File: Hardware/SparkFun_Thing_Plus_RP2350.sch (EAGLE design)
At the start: 78 parts, among them J1 THING_PLUS_LOGICAL, J3 QWIIC_RIGHT_ANGLE, J6 MICRO-SDFRICTION, Q1 100mA/20V/3.8Ω, U1 RP2350A, U2 RM2, U3 RT9080-33GJ5, U4 LM66200, U5 W25QXX128MBIT, U6 MCP73831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

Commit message: Update Eagle libs
Add PROD_ID for RM2
Update Eagle libs for updated version of RT9080 and LM66200
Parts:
- U3: device SparkFun-IC-Power:V_REG_RT9080 -> SparkFun-IC-Power:V_REG_RT9080-33GJ5
- U4: device SparkFun_Thing_Plus_RA6M5:IDEAL_DIODE_DUAL_LM66200 -> SparkFun-IC-Power:IDEAL_DIODE_DUAL_LM66200
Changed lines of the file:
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@@
 <part name="I2C" library="SparkFun-Jumpers" deviceset="JUMPER-SMT_3_2-NC_TRACE" device="_SILK" package3d_urn="urn:adsk.eagle:package:39289/1"/>
 <part name="SUPPLY11" library="SparkFun-PowerSymbols" deviceset="3.3V" device=""/>
-<part name="U3" library="SparkFun-IC-Power" deviceset="V_REG_RT9080" device="" value="RT9080-33GJ5"/>
+<part name="U3" library="SparkFun-IC-Power" deviceset="V_REG_RT9080-33GJ5" device="" value="RT9080-33GJ5"/>
 <part name="C1" library="SparkFun-Capacitors" deviceset="2.2UF" device="-0402_TIGHT-10V-10%-X5R" value="2.2uF"/>
 <part name="C2" library="SparkFun-Capacitors" deviceset="2.2UF" device="-0402_TIGHT-10V-10%-X5R" value="2.2uF"/>
@@
 <part name="SUPPLY12" library="SparkFun-PowerSymbols" deviceset="3.3V" device=""/>
 <part name="R7" library="SparkFun-Resistors" deviceset="1MOHM" device="-0402T-1/16W-5%" value="1M"/>
-<part name="U4" library="SparkFun_Thing_Plus_RA6M5" deviceset="IDEAL_DIODE_DUAL_LM66200" device="" value="LM66200"/>
+<part name="U4" library="SparkFun-IC-Power" deviceset="IDEAL_DIODE_DUAL_LM66200" device="" value="LM66200"/>
 <part name="GND14" library="SparkFun-PowerSymbols" deviceset="GND" device=""/>
 <part name="R8" library="SparkFun-Resistors" deviceset="10KOHM" device="-0402T-1/16W-1%" value="10k"/>

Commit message: Remove SD card SDIO
SDIO can only be achieved via the PIO, and support for it is questionable. Changing to SPI frees up 5 GPIO that can be used for other purposes.
Change SD card socket to CONN-20948
Connect SPI pins to SD card socket
Connect SD card detection pin to GPIO pin
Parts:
- J6: value MICRO-SDFRICTION -> MICRO-SD-ATOM; device SparkFun-Connectors:MICRO-SDFRICTION -> SparkFun-Connectors:MICRO-SD-ATOM
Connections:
- net SD_!CS!/D3 renamed SD_!CS!
- removed net SD_D1: J6.DAT1, U1.GPIO11
- removed net SD_D2: J6.DAT2, U1.GPIO10
- removed net SD_PICO/CMD: J6.CMD/SDI, U1.GPIO15
- removed net SD_POCI/D0: J6.DAT0/SDO, U1.GPIO12
- removed net SD_SCLK: J6.CLK/SCK, U1.GPIO14
- new net !SD_DET!: J6.!DET!, U1.GPIO10
- net 3.3V: now also J6.VDD; no longer J6.VCC
- net GND: now also J6.SHIELD, J6.VSS; no longer J6.GND
- net PICO: now also J6.CMD/SDI
- net POCI: now also J6.DAT0/SDO
- net SCK: now also J6.CLK/SCK
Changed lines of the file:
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@@
 <part name="SUPPLY37" library="SparkFun-PowerSymbols" deviceset="VDDA" device=""/>
 <part name="L1" library="SparkFun-Coils" deviceset="4.7μH_SHIELDED_INDUCTOR" device="" value="4.7μH"/>
-<part name="J6" library="SparkFun-Connectors" deviceset="MICRO-SD" device="FRICTION"/>
 <part name="R18" library="SparkFun-Resistors" deviceset="10OHM" device="-0402-1/16W-5%" value="10Ω"/>
 <part name="C22" library="SparkFun-Capacitors" deviceset="2.2UF" device="-0402_TIGHT-10V-10%-X5R" value="2.2uF"/>
@@
 <part name="R20" library="SparkFun-Resistors" deviceset="10KOHM" device="-0402T-1/16W-1%" value="10k"/>
 <part name="GND41" library="SparkFun-PowerSymbols" deviceset="GND" device=""/>
+<part name="J6" library="SparkFun-Connectors" deviceset="MICRO-SD-ATOM" device=""/>
 </parts>
 <sheets>
@@
 <attribute name="VALUE" x="151.13" y="164.592" size="1.778" layer="96" font="vector" align="top-left"/>
 </instance>
-<instance part="J6" gate="J1" x="289.56" y="180.34" smashed="yes">
-<attribute name="NAME" x="284.48" y="193.548" size="1.778" layer="95"/>
-<attribute name="VALUE" x="284.48" y="165.1" size="1.778" layer="96"/>
-</instance>
 <instance part="R18" gate="G$1" x="170.18" y="81.28" smashed="yes" rot="R180">
 <attribute name="NAME" x="170.18" y="79.756" size="1.778" layer="95" font="vector" rot="R180" align="bottom-center"/>
@@
 <attribute name="VALUE" x="279.4" y="164.846" size="1.778" layer="96" font="vector" align="top-center"/>
 </instance>
-<instance part="SUPPLY40" gate="G$1" x="279.4" y="193.04" smashed="yes">
-<attribute name="VALUE" x="279.4" y="195.834" size="1.778" layer="96" font="vector" align="bottom-center"/>
+<instance part="SUPPLY40" gate="G$1" x="279.4" y="195.58" smashed="yes">
+<attribute name="VALUE" x="279.4" y="198.374" size="1.778" layer="96" font="vector" align="bottom-center"/>
 </instance>
 <instance part="SUPPLY41" gate="G$1" x="347.98" y="132.08" smashed="yes">
@@
 <instance part="GND41" gate="1" x="177.8" y="241.3" smashed="yes">
 <attribute name="VALUE" x="177.8" y="241.046" size="1.778" layer="96" font="vector" align="top-center"/>
+</instance>
+<instance part="J6" gate="G$1" x="292.1" y="180.34" smashed="yes">
+<attribute name="NAME" x="284.48" y="196.088" size="1.778" layer="95" font="vector"/>
+<attribute name="VALUE" x="284.48" y="165.1" size="1.778" layer="96" font="vector"/>
 </instance>
 </instances>
@@
 <segment>
 <pinref part="GND43" gate="1" pin="GND"/>
-<pinref part="J6" gate="J1" pin="GND"/>
 <wire x1="279.4" y1="167.64" x2="279.4" y2="170.18" width="0.1524" layer="91"/>
 <wire x1="279.4" y1="170.18" x2="281.94" y2="170.18" width="0.1524" layer="91"/>
+<pinref part="J6" gate="G$1" pin="VSS"/>
+<pinref part="J6" gate="G$1" pin="SHIELD"/>
+<wire x1="279.4" y1="170.18" x2="279.4" y2="172.72" width="0.1524" layer="91"/>
+<wire x1="279.4" y1="172.72" x2="281.94" y2="172.72" width="0.1524" layer="91"/>
+<junction x="279.4" y="170.18"/>
 </segment>
 <segment>
@@
 </segment>
 <segment>
-<pinref part="J6" gate="J1" pin="VCC"/>
 <pinref part="SUPPLY40" gate="G$1" pin="3.3V"/>
-<wire x1="281.94" y1="190.5" x2="279.4" y2="190.5" width="0.1524" layer="91"/>
-<wire x1="279.4" y1="190.5" x2="279.4" y2="193.04" width="0.1524" layer="91"/>
+<wire x1="281.94" y1="193.04" x2="279.4" y2="193.04" width="0.1524" layer="91"/>
+<wire x1="279.4" y1="193.04" x2="279.4" y2="195.58" width="0.1524" layer="91"/>
+<pinref part="J6" gate="G$1" pin="VDD"/>
 </segment>
 <segment>
@@
 <pinref part="U1" gate="G$1" pin="GPIO4"/>
 </segment>
+<segment>
+<wire x1="281.94" y1="180.34" x2="279.4" y2="180.34" width="0.1524" layer="91"/>
+<label x="279.4" y="180.34" size="1.27" layer="95" font="vector" rot="R180" xref="yes"/>
+<pinref part="J6" gate="G$1" pin="DAT0/SDO"/>
+</segment>
 </net>
 <net name="PICO" class="0">
@@
 <pinref part="U1" gate="G$1" pin="GPIO3"/>
 </segment>
+<segment>
+<wire x1="281.94" y1="175.26" x2="279.4" y2="175.26" width="0.1524" layer="91"/>
+<label x="279.4" y="175.26" size="1.27" layer="95" font="vector" rot="R180" xref="yes"/>
+<pinref part="J6" gate="G$1" pin="CMD/SDI"/>
+</segment>
 </net>
 <net name="SCK" class="0">
@@
 <label x="200.66" y="175.26" size="1.27" layer="95" font="vector" xref="yes"/>
 <pinref part="U1" gate="G$1" pin="GPIO2"/>
+</segment>
+<segment>
+<wire x1="281.94" y1="177.8" x2="279.4" y2="177.8" width="0.1524" layer="91"/>
+<label x="279.4" y="177.8" size="1.27" layer="95" font="vector" rot="R180" xref="yes"/>
+<pinref part="J6" gate="G$1" pin="CLK/SCK"/>
 </segment>
 </net>
@@
 </segment>
 </net>
-<net name="SD_!CS!/D3" class="0">
-<segment>
-<pinref part="J6" gate="J1" pin="DAT3/!CS!"/>
+<net name="SD_!CS!" class="0">
+<segment>
 <wire x1="281.94" y1="187.96" x2="279.4" y2="187.96" width="0.1524" layer="91"/>
 <label x="279.4" y="187.96" size="1.27" layer="95" font="vector" rot="R180" xref="yes"/>
+<pinref part="J6" gate="G$1" pin="DAT3/!CS!"/>
 </segment>
 <segment>
@@
 <label x="200.66" y="157.48" size="1.27" layer="95" font="vector" rot="MR180" xref="yes"/>
 <pinref part="U1" gate="G$1" pin="GPIO9"/>
-</segment>
-</net>
-<net name="SD_D2" class="0">
-<segment>
-<pinref part="J6" gate="J1" pin="DAT2"/>
-<wire x1="281.94" y1="185.42" x2="279.4" y2="185.42" width="0.1524" layer="91"/>
-<label x="279.4" y="185.42" size="1.27" layer="95" font="vector" rot="R180" xref="yes"/>
-</segment>
-<segment>
-<wire x1="198.12" y1="154.94" x2="200.66" y2="154.94" width="0.1524" layer="91"/>
-<label x="200.66" y="154.94" size="1.27" layer="95" font="vector" rot="MR180" xref="yes"/>
-<pinref part="U1" gate="G$1" pin="GPIO10"/>
-</segment>
-</net>
-<net name="SD_D1" class="0">
-<segment>
-<pinref part="J6" gate="J1" pin="DAT1"/>
-<wire x1="281.94" y1="182.88" x2="279.4" y2="182.88" width="0.1524" layer="91"/>
-<label x="279.4" y="182.88" size="1.27" layer="95" font="vector" rot="R180" xref="yes"/>
-</segment>
-<segment>
-<wire x1="198.12" y1="152.4" x2="200.66" y2="152.4" width="0.1524" layer="91"/>
-<label x="200.66" y="152.4" size="1.27" layer="95" font="vector" rot="MR180" xref="yes"/>
-<pinref part="U1" gate="G$1" pin="GPIO11"/>
-</segment>
-</net>
-<net name="SD_POCI/D0" class="0">
-<segment>
-<pinref part="J6" gate="J1" pin="DAT0/SDO"/>
-<wire x1="281.94" y1="180.34" x2="279.4" y2="180.34" width="0.1524" layer="91"/>
-<label x="279.4" y="180.34" size="1.27" layer="95" font="vector" rot="R180" xref="yes"/>
-</segment>
-<segment>
-<wire x1="198.12" y1="149.86" x2="200.66" y2="149.86" width="0.1524" layer="91"/>
-<label x="200.66" y="149.86" size="1.27" layer="95" font="vector" rot="MR180" xref="yes"/>
-<pinref part="U1" gate="G$1" pin="GPIO12"/>
-</segment>
-</net>
-<net name="SD_SCLK" class="0">
-<segment>
-<pinref part="J6" gate="J1" pin="CLK/SCK"/>
-<wire x1="281.94" y1="177.8" x2="279.4" y2="177.8" width="0.1524" layer="91"/>
-<label x="279.4" y="177.8" size="1.27" layer="95" font="vector" rot="R180" xref="yes"/>
-</segment>
-<segment>
-<wire x1="198.12" y1="144.78" x2="200.66" y2="144.78" width="0.1524" layer="91"/>
-<label x="200.66" y="144.78" size="1.27" layer="95" font="vector" rot="MR180" xref="yes"/>
-<pinref part="U1" gate="G$1" pin="GPIO14"/>
-</segment>
-</net>
-<net name="SD_PICO/CMD" class="0">
-<segment>
-<pinref part="J6" gate="J1" pin="CMD/SDI"/>
-<wire x1="281.94" y1="175.26" x2="279.4" y2="175.26" width="0.1524" layer="91"/>
-<label x="279.4" y="175.26" size="1.27" layer="95" font="vector" rot="R180" xref="yes"/>
-</segment>
-<segment>
-<wire x1="198.12" y1="142.24" x2="200.66" y2="142.24" width="0.1524" layer="91"/>
-<label x="200.66" y="142.24" size="1.27" layer="95" font="vector" rot="MR180" xref="yes"/>
-<pinref part="U1" gate="G$1" pin="GPIO15"/>
 </segment>
 </net>
@@
 </segment>
 </net>
+<net name="!SD_DET!" class="0">
+<segment>
+<pinref part="J6" gate="G$1" pin="!DET!"/>
+<wire x1="281.94" y1="190.5" x2="279.4" y2="190.5" width="0.1524" layer="91"/>
+<label x="279.4" y="190.5" size="1.27" layer="95" font="vector" rot="R180" xref="yes"/>
+</segment>
+<segment>
+<wire x1="198.12" y1="154.94" x2="200.66" y2="154.94" width="0.1524" layer="91"/>
+<label x="200.66" y="154.94" size="1.27" layer="95" font="vector" xref="yes"/>
+<pinref part="U1" gate="G$1" pin="GPIO10"/>
+</segment>
+</net>

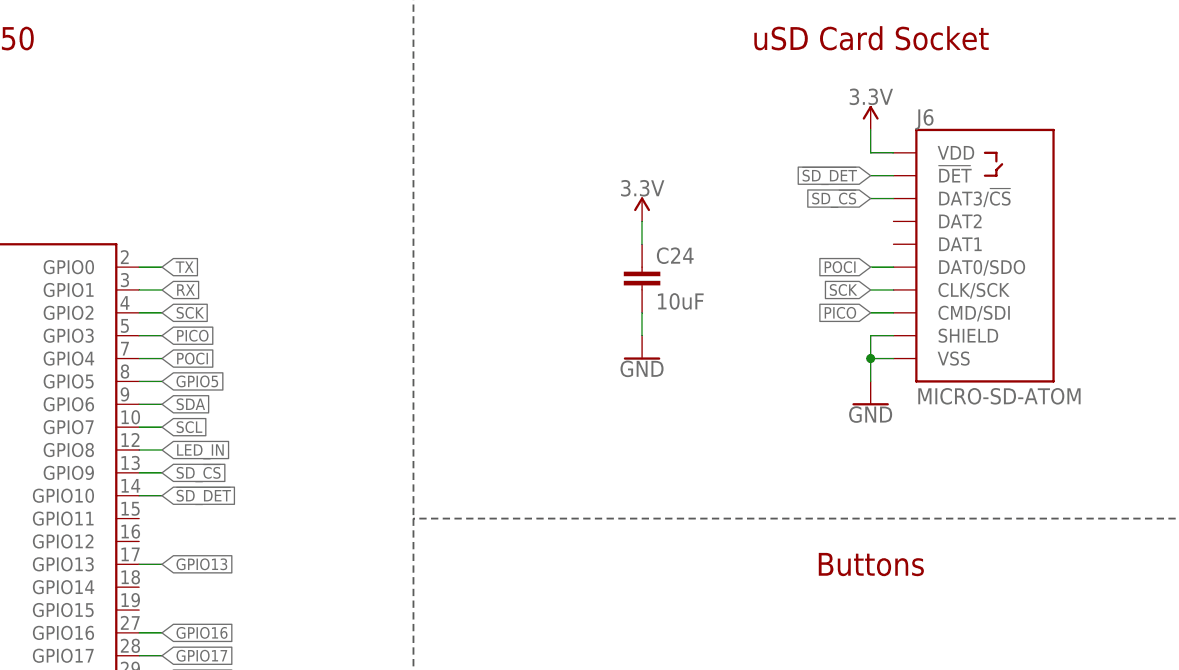
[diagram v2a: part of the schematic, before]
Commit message: Fix SD card detection being active high
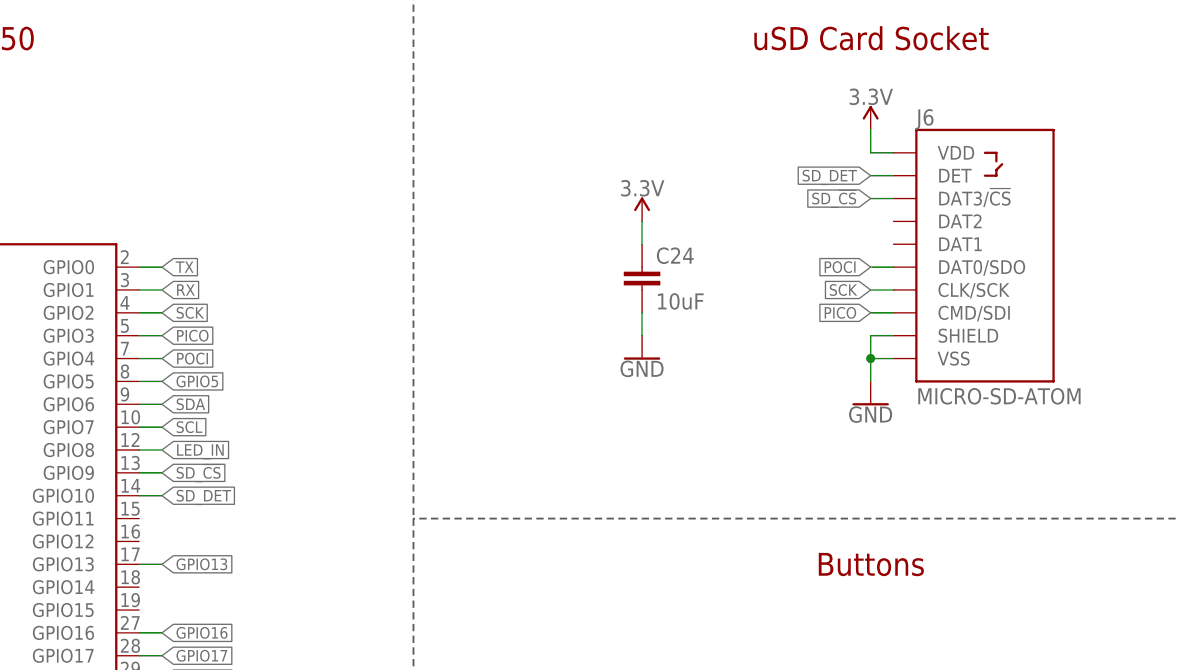
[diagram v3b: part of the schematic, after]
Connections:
- removed net !SD_DET!: J6.!DET!, U1.GPIO10
- new net SD_DET: J6.DET, U1.GPIO10
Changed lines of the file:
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@@
 </segment>
 </net>
-<net name="!SD_DET!" class="0">
+<net name="SD_DET" class="0">
 <segment>
-<pinref part="J6" gate="G$1" pin="!DET!"/>
+<pinref part="J6" gate="G$1" pin="DET"/>
 <wire x1="281.94" y1="190.5" x2="279.4" y2="190.5" width="0.1524" layer="91"/>
 <label x="279.4" y="190.5" size="1.27" layer="95" font="vector" rot="R180" xref="yes"/>

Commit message: Add peripheral power control
Add a second voltage regulator dedicated to powering the WS2812, uSD card, and Qwiic connector
Change pinout of A4 and A5 of Thing Plus pinout to make routing easier, and replace RM2 GPIO with RP2350 GPIO
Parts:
- added C13: 2.2uF, SparkFun-Capacitors:2.2UF-0402_TIGHT-10V-10%-X5R
- added C25: 0.1uF, SparkFun-Capacitors:0.1UF-0402T-6.3V-10%-X7R
- added LP: JUMPER-SMT_2_NC_TRACE_SILK, SparkFun-Jumpers:JUMPER-SMT_2_NC_TRACE_SILK
- added R21: 10k, SparkFun-Resistors:10KOHM-0402T-1/16W-1%
- added R22: 1M, SparkFun-Resistors:1MOHM-0402T-1/16W-5%
- added U9: RT9080-33GJ5, SparkFun-IC-Power:V_REG_RT9080-33GJ5
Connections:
- removed net GPIO13: J1.A4, U1.GPIO13
- removed net WL_GPIO1: J1.A5, U2.GPIO1
- new net 3.3V_SW: C24.1, C25.1, I2C.2, J3.2, J6.VDD, U7.VCC, U9.OUT
- new net GPIO11: J1.A4, U1.GPIO11
- new net GPIO12: J1.A5, U1.GPIO12
- new net PERIPH_POW: R21.1, R22.2, U1.GPIO13, U9.EN
- new net VIN: C1.1, C13.1, R7.1, U3.IN, U4.VOUT, U9.IN
- net 3.3V: now also LP.2; no longer C24.1, I2C.2, J3.2, J6.VDD, U7.VCC
- net GND: now also C13.2, C25.2, R22.1, U9.GND
- net N$11: now also LP.1, R21.2; no longer C1.1, R7.1, U3.IN, U4.VOUT
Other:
- note added: "Cut LP jumper to make peripherals default to off"
- note added: "Peripheral Power Control"
- moved on the sheet: BOOT, C24, J5, R12, RESET

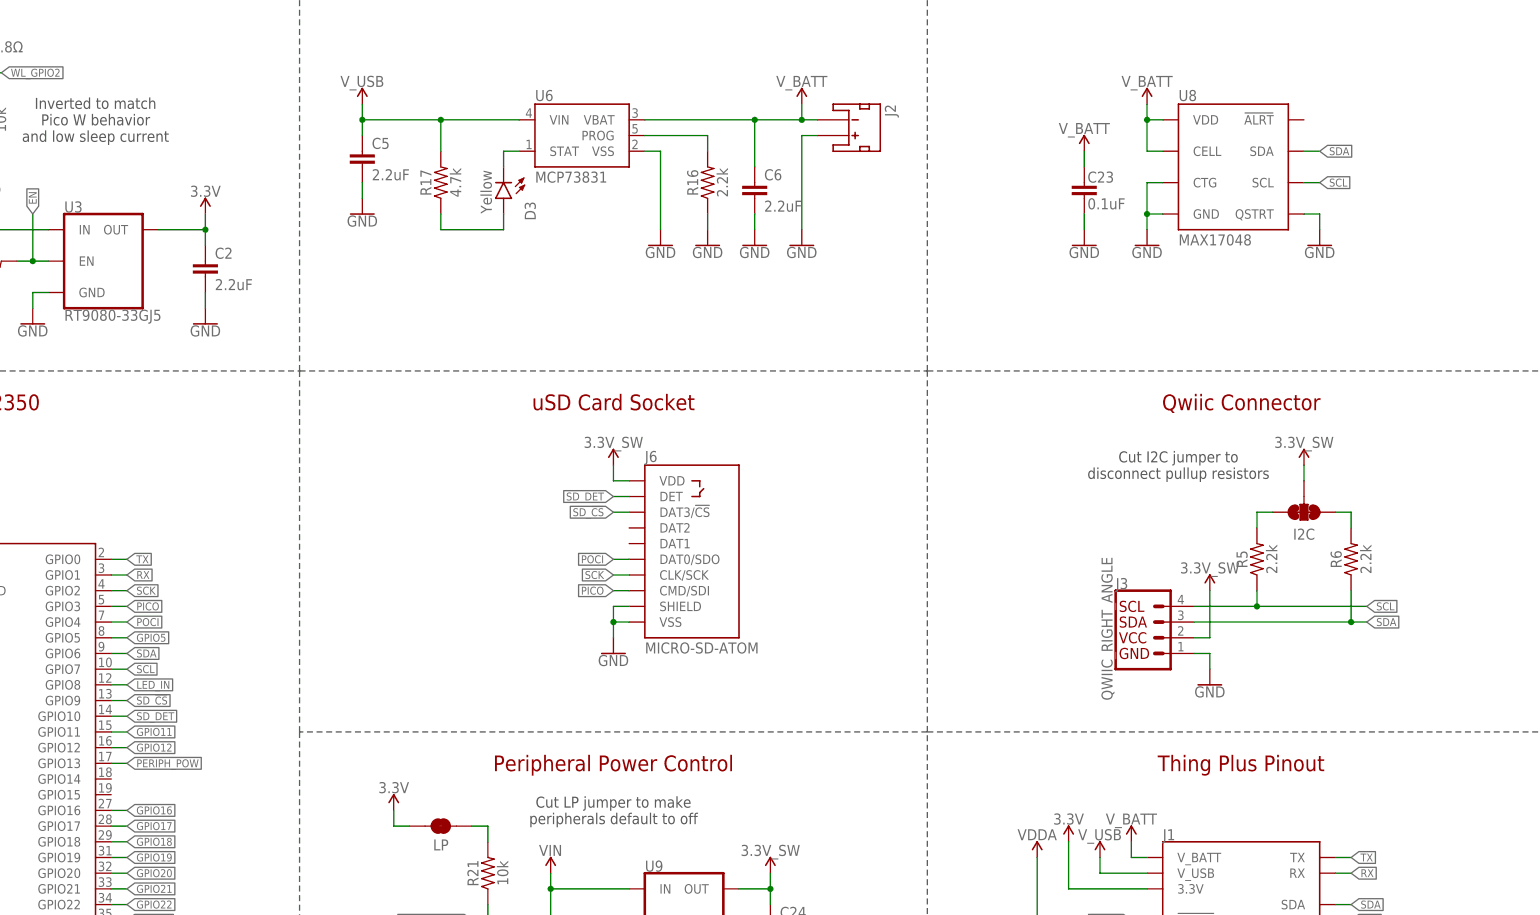
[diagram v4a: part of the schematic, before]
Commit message: Connect fuel gauge alert pin
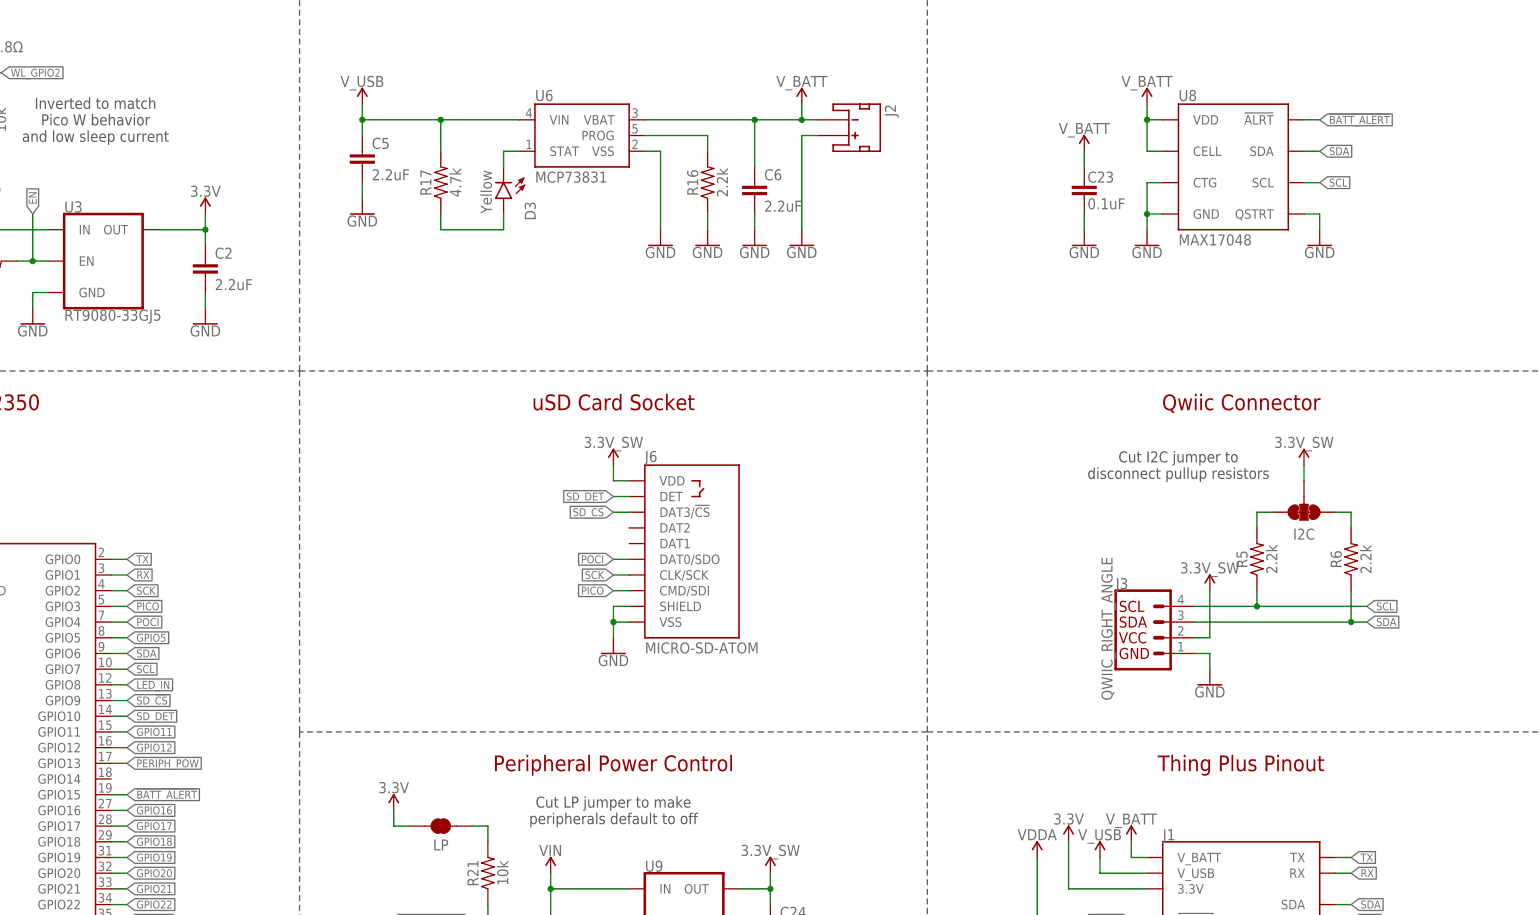
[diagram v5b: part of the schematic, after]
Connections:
- new net !BATT_ALERT!: U1.GPIO15, U8.!ALRT
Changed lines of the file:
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@@
+</segment>
+</net>
+<net name="!BATT_ALERT!" class="0">
+<segment>
+<pinref part="U8" gate="U1" pin="!ALRT"/>
+<wire x1="391.16" y1="251.46" x2="393.7" y2="251.46" width="0.1524" layer="91"/>
+<label x="393.7" y="251.46" size="1.27" layer="95" font="vector" xref="yes"/>
+</segment>
+<segment>
+<wire x1="198.12" y1="142.24" x2="200.66" y2="142.24" width="0.1524" layer="91"/>
+<label x="200.66" y="142.24" size="1.27" layer="95" font="vector" xref="yes"/>
+<pinref part="U1" gate="G$1" pin="GPIO15"/>
 </segment>
 </net>
